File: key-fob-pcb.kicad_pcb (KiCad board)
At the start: 2 copper layers, 30.5 x 63.5 mm, 24 parts, among them J1 Programming Jumper, J2 Programming Header, Q1 IRLML6402TRPBF, SW1 START/STOP BTN, SW2 EN, U1 ESP32-S3-MINI-1, U2 TPS61023DRLT, U3 IRLML2502TRPBF

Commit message: add 3D models and generate STEP file for PCB
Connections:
- net /VCC renamed /ESP32/VCC
- C1 pad 2: /ADC/GND -> GND
- C2 pad 2: /ADC/GND -> GND
- J1 pad 2: /ADC/GND -> GND
- J2 pad 3: /ADC/GND -> GND
- R1 pad 1: /ADC/GND -> GND
- R13 pad 2: /ADC/GND -> GND
- R4 pad 2: /ADC/GND -> GND
- R7 pad 1: /ADC/GND -> GND
- R8 pad 1: /ADC/GND -> GND
- R9 pad 1: /ADC/GND -> GND
- SW2 pad 1: /ADC/GND -> GND
- U1 pad 1: /ADC/GND -> GND
- U1 pad 2: /ADC/GND -> GND
- U1 pad 42: /ADC/GND -> GND
- U1 pad 43: /ADC/GND -> GND
- U1 pad 46: /ADC/GND -> GND
- U1 pad 47: /ADC/GND -> GND
- U1 pad 48: /ADC/GND -> GND
- U1 pad 49: /ADC/GND -> GND
- U1 pad 50: /ADC/GND -> GND
- U1 pad 51: /ADC/GND -> GND
- U1 pad 52: /ADC/GND -> GND
- U1 pad 53: /ADC/GND -> GND
- U1 pad 54: /ADC/GND -> GND
- U1 pad 55: /ADC/GND -> GND
- U1 pad 56: /ADC/GND -> GND
- U1 pad 57: /ADC/GND -> GND
- U1 pad 58: /ADC/GND -> GND
- U1 pad 59: /ADC/GND -> GND
- U1 pad 60: /ADC/GND -> GND
- U1 pad 61: /ADC/GND -> GND
- U1 pad 62: /ADC/GND -> GND
- U1 pad 63: /ADC/GND -> GND
- U1 pad 64: /ADC/GND -> GND
- U1 pad 65: /ADC/GND -> GND
- U2 pad 4: /ADC/GND -> GND
- U3 pad 2: /ADC/GND -> GND
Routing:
- net GND: track 0.00 -> 21.8 mm, vias 0 -> 25
- net /ADC/GND: track 21.8 -> 0.00 mm, vias 25 -> 0
- added copper zone on B.Cu, net GND
- added copper zone on F.Cu, net GND
- removed copper zone on B.Cu, net /ADC/GND
- removed copper zone on F.Cu, net /ADC/GND

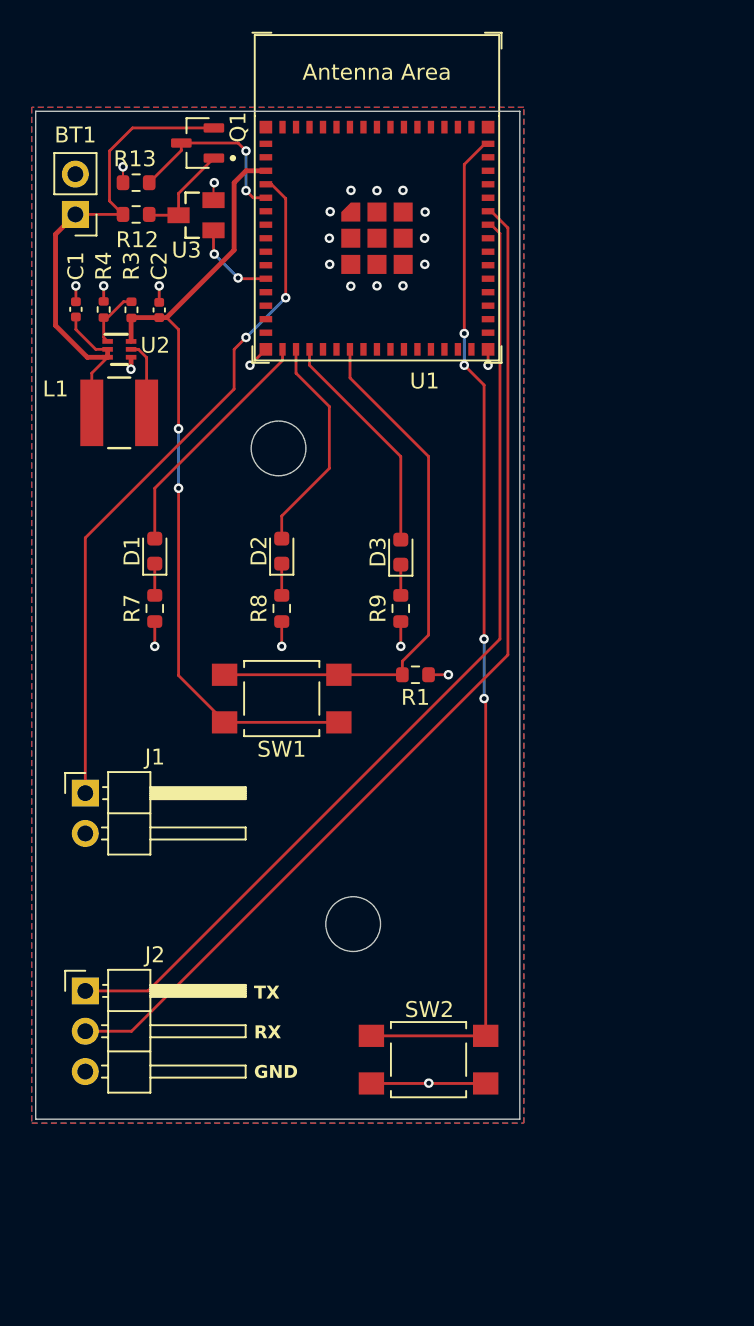
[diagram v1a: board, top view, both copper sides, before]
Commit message: switched to full-sized ESP32 S3 WROOM and redid PCB layout
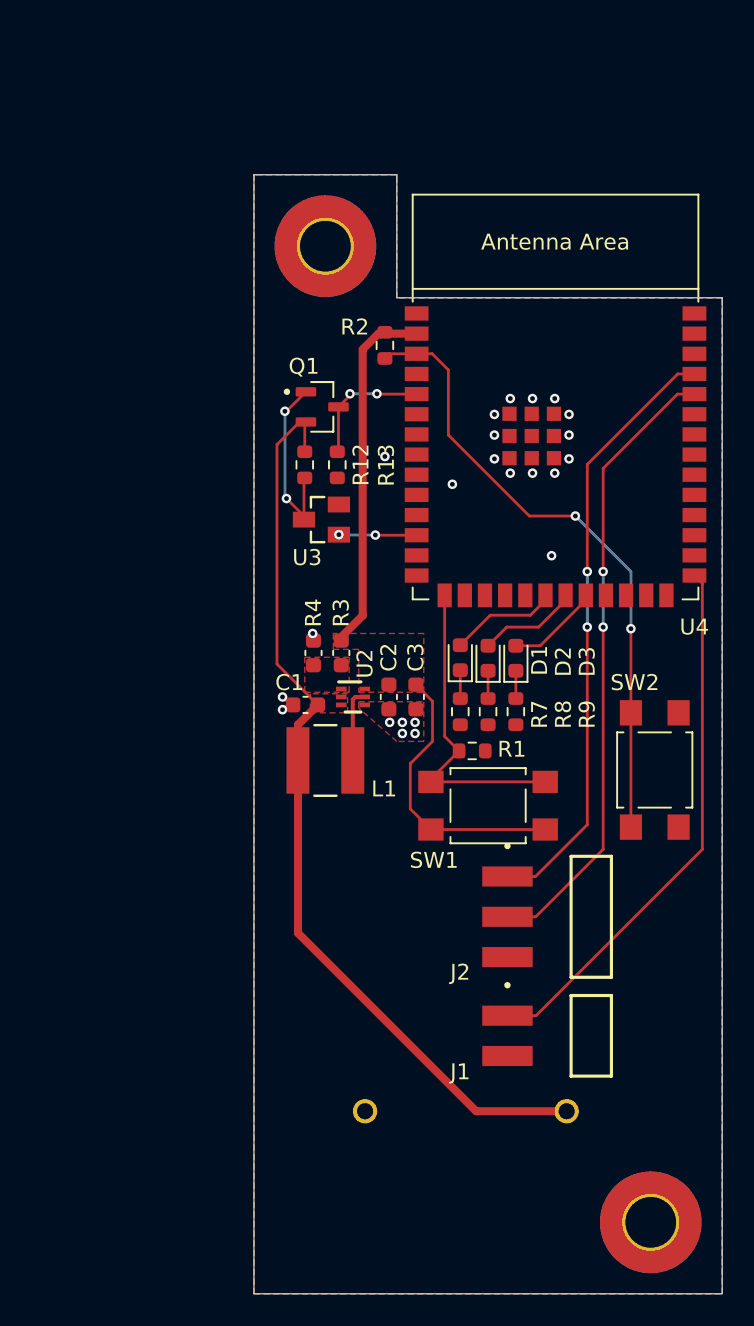
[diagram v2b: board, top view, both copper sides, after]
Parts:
- removed Battery Holder: BAT_2468, 2469:BAT_2469
- removed U1: ESP32-S3-MINI-1, PCM_Espressif:ESP32-S3-MINI-1
- added C3: 22u, Capacitor_SMD:C_0603_1608Metric, F.Cu at (148.4, 119.4)
- added R2: 10k, Resistor_SMD:R_0603_1608Metric, F.Cu at (146.5, 97.2)
- added REF**: MountingHole_3.2mm_M3_Pad_TopBottom, MountingHole:MountingHole_3.2mm_M3_Pad_TopBottom, F.Cu at (163.2, 152.5)
- added REF**: MountingHole_3.2mm_M3_Pad_TopBottom, MountingHole:MountingHole_3.2mm_M3_Pad_TopBottom, F.Cu at (142.8, 91.0)
- added U4: ESP32-S3-WROOM-1, PCM_Espressif:ESP32-S3-WROOM-1, F.Cu at (157.2, 103.5)
- BT1: value AAAx2 -> 2468; footprint Connector_PinHeader_2.54mm:PinHeader_1x02_P2.54mm_Vertical -> 2468:BAT_2468; moved to B.Cu
- C1: footprint Capacitor_SMD:C_0402_1005Metric -> Capacitor_SMD:C_0603_1608Metric
- C2: value 4.7u -> 22u; footprint Capacitor_SMD:C_0402_1005Metric -> Capacitor_SMD:C_0603_1608Metric
- J1: footprint Connector_PinHeader_2.54mm:PinHeader_1x02_P2.54mm_Horizontal -> SAMTEC_TSM-102-01-L-SH:SAMTEC_TSM-102-01-L-SH
- J2: footprint Connector_PinHeader_2.54mm:PinHeader_1x03_P2.54mm_Horizontal -> SAMTEC_TSM-103-01-L-SH-TR:SAMTEC_TSM-103-01-L-SH-TR
- R3, R4: footprint Resistor_SMD:R_0402_1005Metric -> Capacitor_SMD:C_0603_1608Metric
- moved BT1 40.8 mm to (151.6, 121.6), turned to -90 degrees
- moved J1 35.4 mm to (159.5, 140.8), turned to -90 degrees
- moved J2 32.2 mm to (159.5, 133.2), turned to -90 degrees
- moved C1 28.8 mm to (141.5, 119.9), turned to 180 degrees
- moved C2 28.3 mm to (146.8, 119.4), turned to -90 degrees
- moved U2 26.4 mm to (144.5, 119.4)
- moved L1 25.5 mm to (142.8, 123.4)
- moved R4 25.4 mm to (142.0, 116.6)
- moved R3 25.3 mm to (143.8, 116.6), turned to -90 degrees
- moved SW2 23.2 mm to (163.5, 124.0), turned to -90 degrees
- moved R13 21.8 mm to (143.5, 104.8), turned to -90 degrees
- moved U3 20.7 mm to (142.5, 108.2)
- moved D1 20.4 mm to (151.2, 116.9)
- moved R7 20.3 mm to (151.2, 120.3)
- moved R12 19.0 mm to (141.4, 104.8), turned to -90 degrees
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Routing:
- net /RX: track 65.0 -> 39.5 mm, vias 0 -> 2
- net /EN: track 64.8 -> 40.0 mm, vias 4 -> 2
- net /TX: track 61.8 -> 38.2 mm, vias 0 -> 2
- net /ADC/VIN: track 34.8 -> 58.3 mm
- net GND: track 21.8 -> 2.15 mm, vias 25 -> 23
- net /START_STOP: track 34.4 -> 20.1 mm
- net /BOOT: track 44.3 -> 34.1 mm, vias 2 -> 0
- net /ESP32/VCC: track 50.5 -> 40.4 mm, vias 2 -> 0
- net /LED3: track 14.4 -> 5.90 mm
- net /LED1: track 15.3 -> 6.84 mm
- net /LED2: track 14.0 -> 6.38 mm
- net Net-(Q1-Pad1): track 7.32 -> 11.8 mm, vias 0 -> 2
- net Net-(U2-FB): track 3.77 -> 0.00 mm
- net /VBAT_ADC: track 11.6 -> 8.19 mm
- net /VBAT_ADC_EN: track 5.46 -> 4.91 mm
- added copper zone on F.Cu, net /ADC/VIN
- added copper zone on F.Cu, net /ESP32/VCC
- added copper zone on F.Cu, net Net-(U2-FB)
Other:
- board size 30.5 x 63.5 mm -> 29.5 x 70.5 mm
- board text added: "Ben Martens 2024-02 Key Fob v2"
- board text removed: "+"
- board text removed: "-"
- board text removed: "Ben Martens 2023-11"
- board text removed: "GND"
- board text removed: "RX"
- board text removed: "TX"
